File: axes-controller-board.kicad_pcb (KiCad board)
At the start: 4 copper layers, 203.1 x 102.9 mm, 173 parts, among them IC1 TPS5450QDDARQ1, IC2 ACS37800KMACTR-030B3-SPI, IC3 ACS37800KMACTR-030B3-SPI, IC4 ACS37800KMACTR-030B3-SPI, IC5 STM32H723ZGT6, J1 Conn_ST_STDC14, J10 Conn_01x08, J11 Conn_01x04, J12 Conn_01x08, J13 Conn_01x04, J14 Conn_01x08, J15 Conn_01x08, J16 Conn_01x04, J17 Conn_01x08, J18 Conn_01x08, J19 Conn_01x04, J2 Conn_01x03, J20 Conn_01x08, J21 Conn_01x08, J22 Conn_01x04, J23 Conn_01x08, J24 Conn_01x08, J25 Conn_01x04, J26 Conn_01x08, J27 Raspberry_Pi_2_3, J28 DC1, J29 DC2, J3 Conn_01x03, J30 DC3, J31 Conn_01x08, J32 Conn_01x08, J33 DC1, J34 Conn_01x08, J35 Conn_01x08, J36 Conn_01x08, J37 ENDSTOP, J38 ENDSTOP, J39 ENDSTOP, J4 Conn_01x03, J40 Conn_01x03, J41 ENDSTOP, J42 ENDSTOP, J5 DRIVER, J6 NTC, J7 DRIVER, J8 NTC, J9 Conn_01x08, SW1 RESET, U1 LM1117MP-3.3, U3 UA9637A, U5 UA9637A, U7 UA9637A, Y1 16MHz

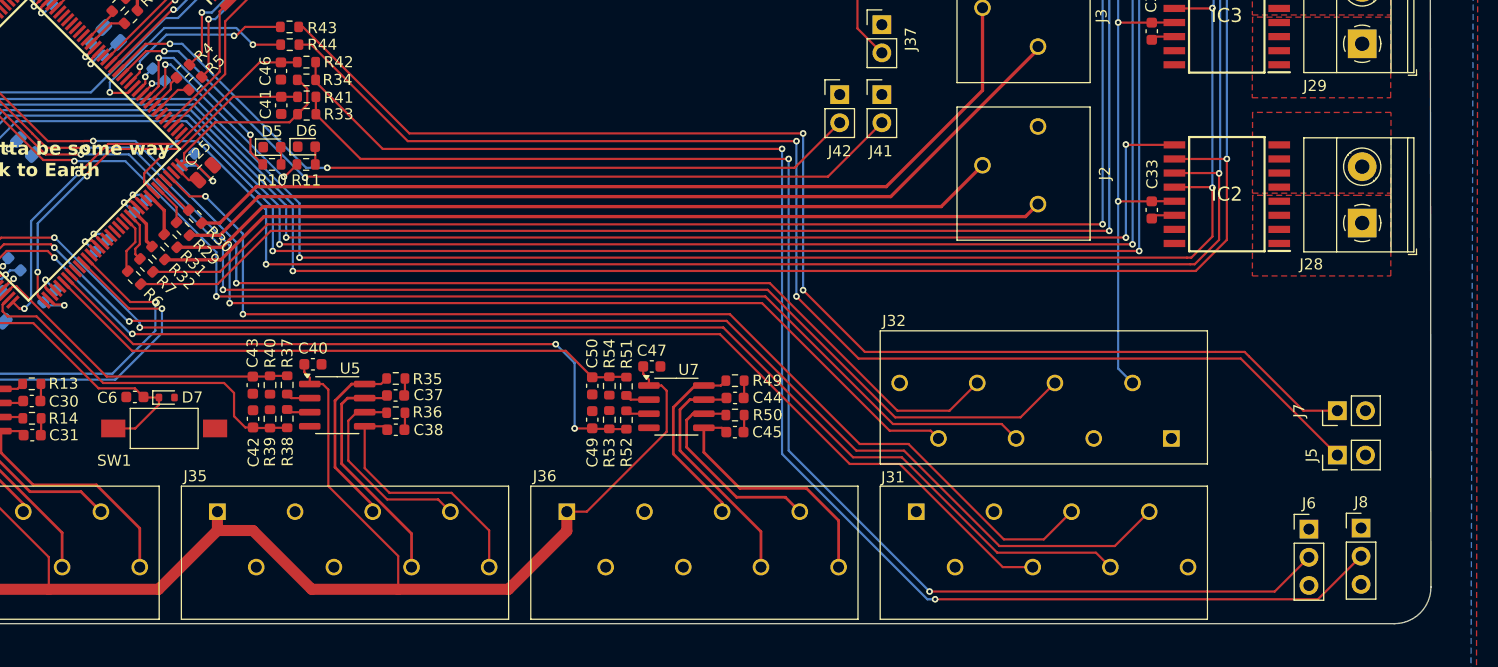
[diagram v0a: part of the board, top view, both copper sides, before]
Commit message: fix: nozzle and hb connector
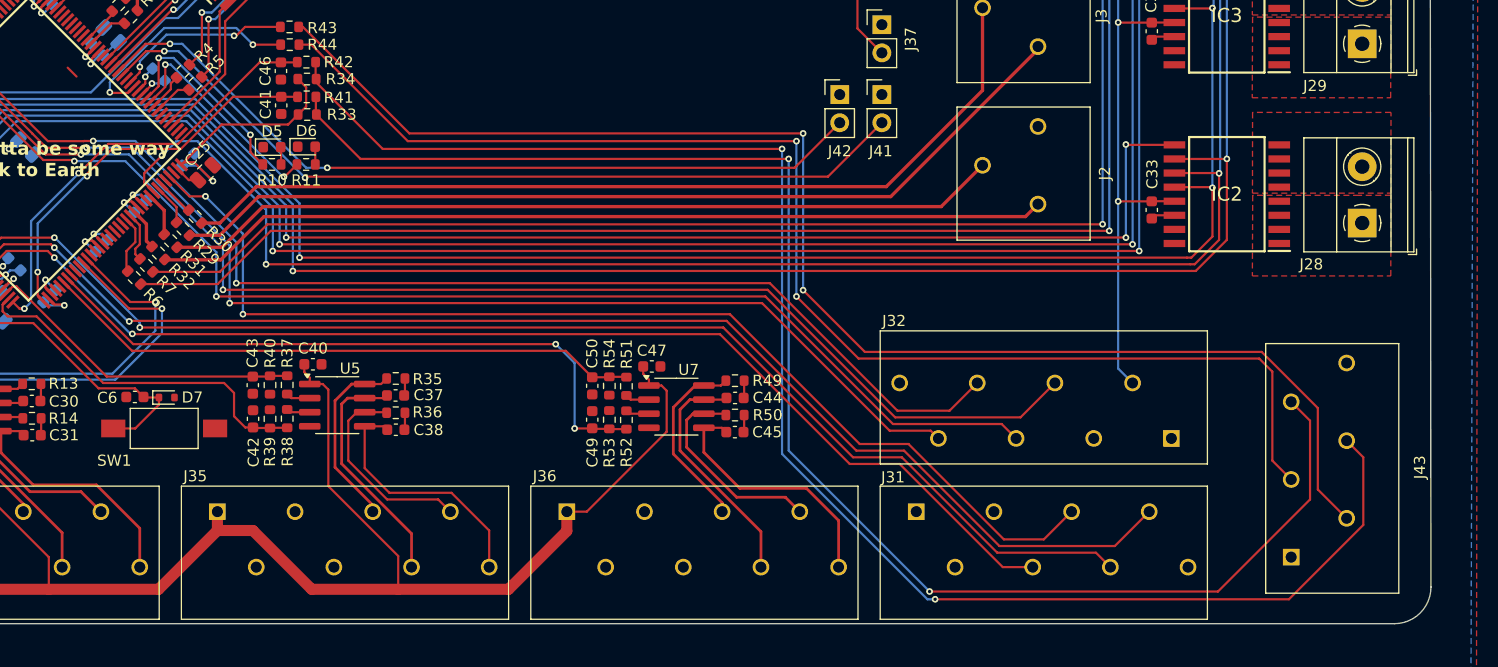
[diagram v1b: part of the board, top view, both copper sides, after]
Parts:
- removed J5, J7: DRIVER, Connector_PinHeader_2.54mm:PinHeader_1x02_P2.54mm_Vertical
- removed J6, J8: NTC, Connector_PinHeader_2.54mm:PinHeader_1x03_P2.54mm_Vertical
- added J43: Conn_01x06, Local:1985234, F.Cu at (250.3, 139.0)
- moved R34 0.09 mm to (161.6, 95.9), turned to 0 degrees
- moved R33 0.06 mm to (161.6, 99.1), turned to 0 degrees
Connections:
- R33 pad 1: Net-(J6-Pin_2) -> +3V3
- R33 pad 2: +3V3 -> Net-(J43-Pin_5)
- R34 pad 1: Net-(J8-Pin_2) -> +3V3
- R34 pad 2: +3V3 -> Net-(J43-Pin_4)
- R41 pad 2: Net-(J6-Pin_2) -> Net-(J43-Pin_5)
- R42 pad 2: Net-(J8-Pin_2) -> Net-(J43-Pin_4)
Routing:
- net Net-(J43-Pin_4): track 0.00 -> 142.7 mm, vias 0 -> 2
- net Net-(J43-Pin_5): track 0.00 -> 137.4 mm, vias 0 -> 2
- net Net-(J8-Pin_2): track 133.1 -> 0.00 mm, vias 2 -> 0
- net Net-(J6-Pin_2): track 125.6 -> 0.00 mm, vias 2 -> 0
- net /N_PWM: track 116.2 -> 125.4 mm
- net /H_PWM: track 117.1 -> 118.6 mm
- net GND: track 51.6 -> 52.7 mm

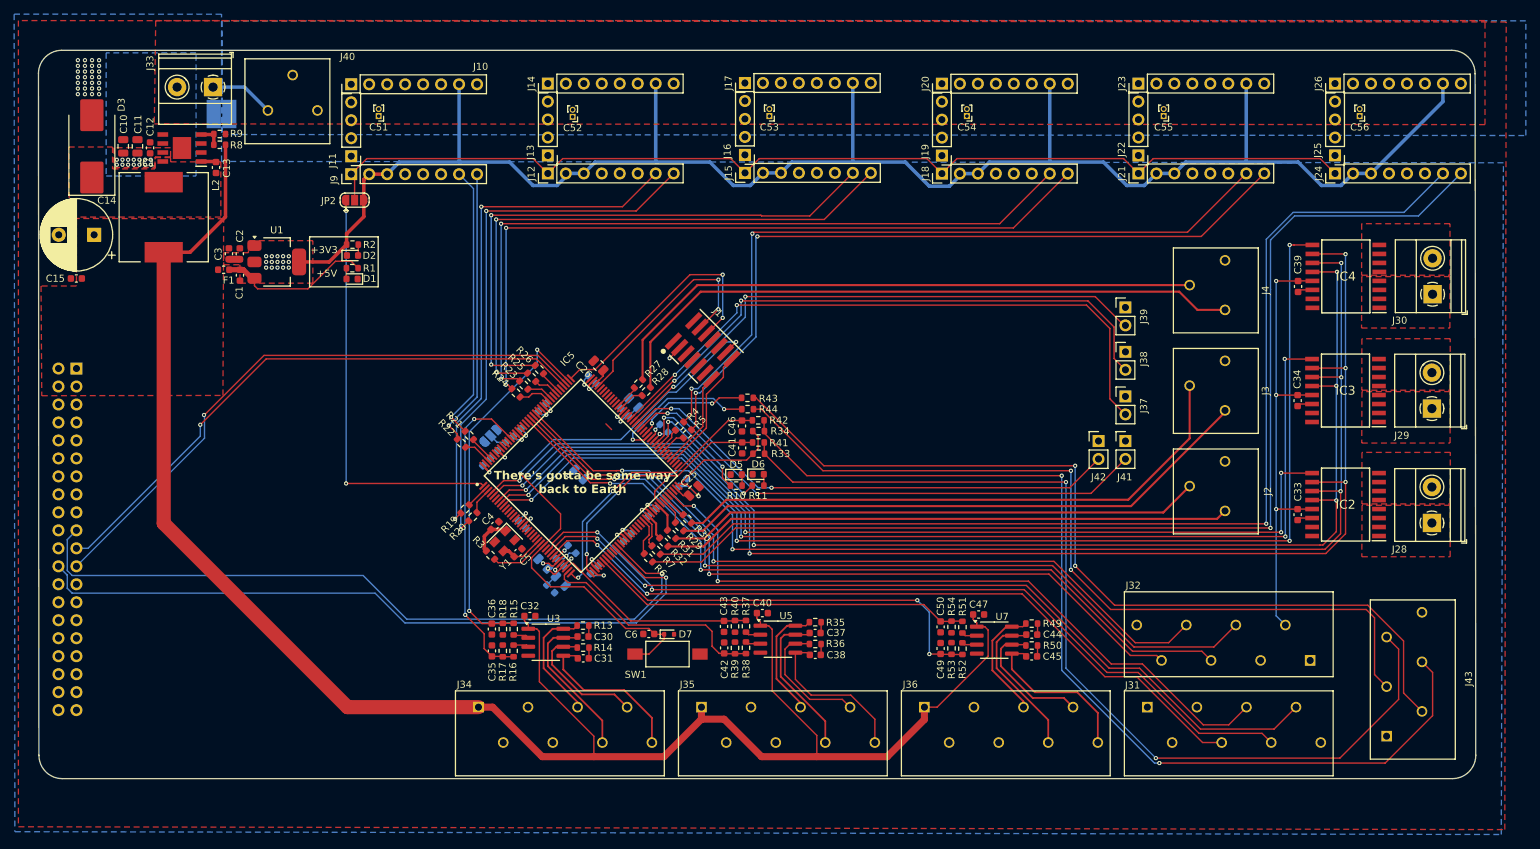
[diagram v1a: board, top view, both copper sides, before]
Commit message: fix: 3d 6 pin connector libs, fix DRC
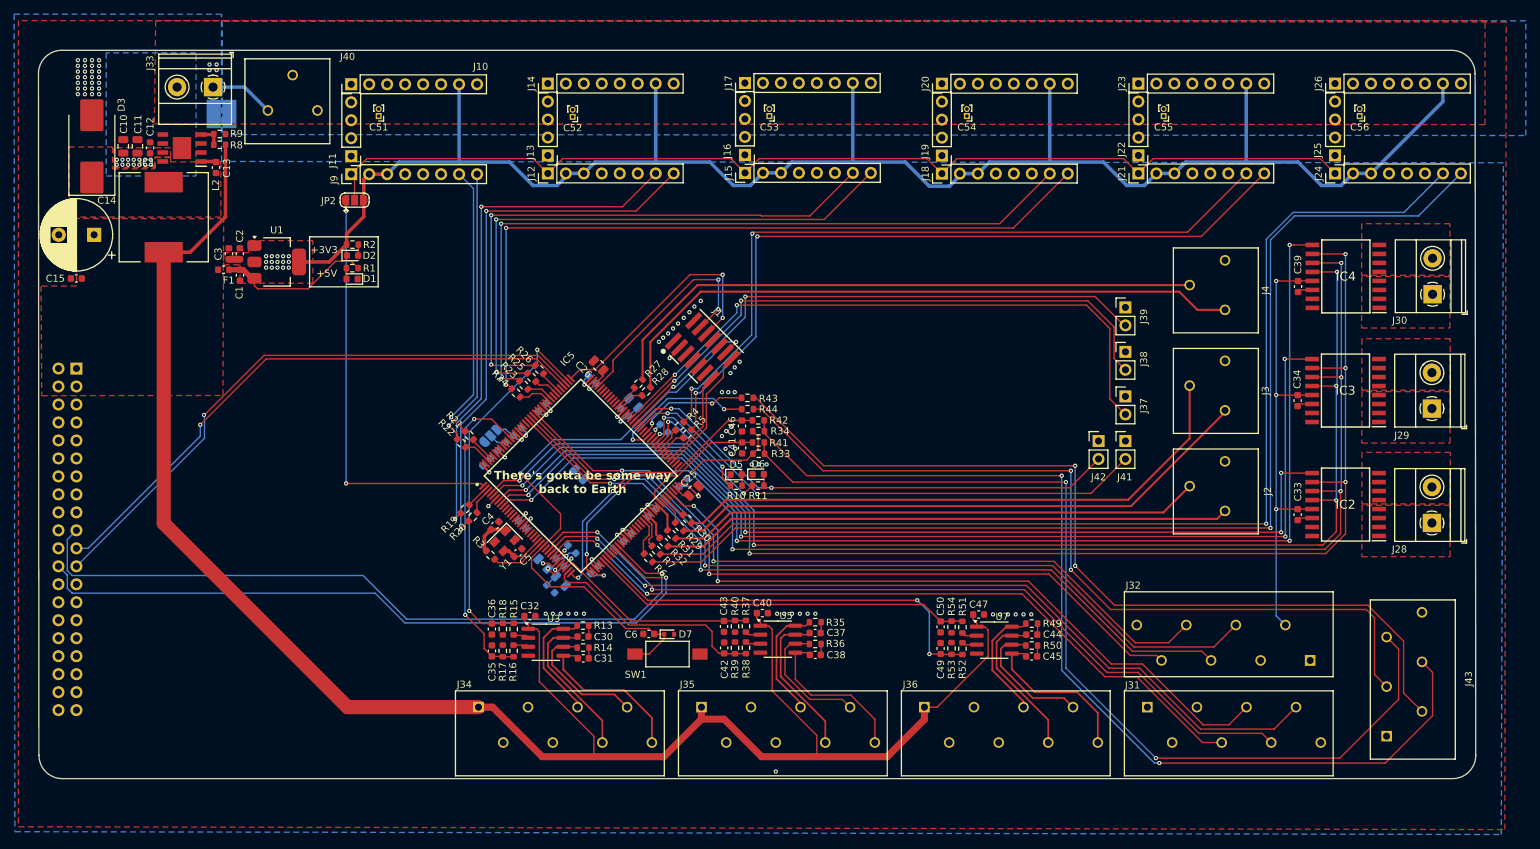
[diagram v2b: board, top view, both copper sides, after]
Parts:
- moved C18 0.16 mm to (127.5, 96.0)
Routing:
- net +3V3: track 381.7 -> 385.9 mm, vias 35 -> 36
- net GND: track 52.7 -> 51.7 mm, vias 39 -> 90

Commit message: feat: mounting holes
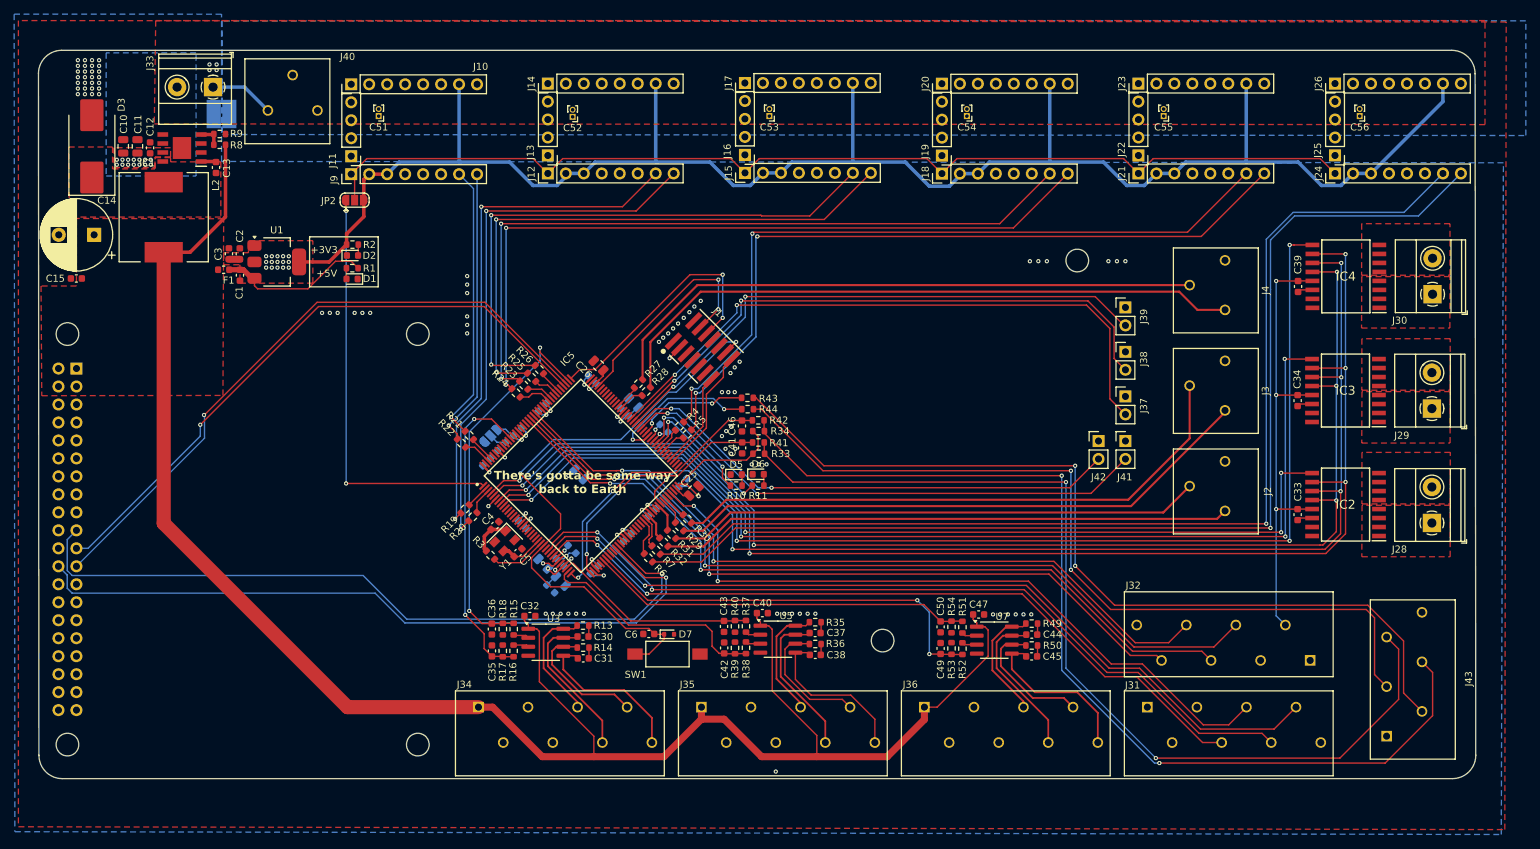
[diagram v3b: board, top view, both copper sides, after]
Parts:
- added H3: MountingHole, Local:MountingHole_3.2mm_M3_ISO14580, F.Cu at (63.9, 140.2)
- added H4: MountingHole, Local:MountingHole_3.2mm_M3_ISO14580, F.Cu at (113.4, 140.2)
- added H5: MountingHole, Local:MountingHole_3.2mm_M3_ISO14580, F.Cu at (113.4, 82.2)
- added H6: MountingHole, Local:MountingHole_3.2mm_M3_ISO14580, F.Cu at (63.9, 82.2)
- added H7: MountingHole, Local:MountingHole_3.2mm_M3_ISO14580, F.Cu at (206.6, 71.8)
- added H8: MountingHole, Local:MountingHole_3.2mm_M3_ISO14580, F.Cu at (179.1, 125.5)
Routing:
- net /MCU/SPI3_SCK: track 85.2 -> 91.4 mm
- net /MCU/SPI3_MISO: track 82.4 -> 88.5 mm
- net /MCU/MX_A: track 54.1 -> 54.7 mm
- net GND: vias 90 -> 108

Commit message: feat: matrix cit
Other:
- board text added: "The spice must flow"
- board text added: "{dblquote}Because you didn't come here to make the choiche, you've already made it. You're here to try to understand why you made it{dblquote}"
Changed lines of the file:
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@@
 		(layer "Edge.Cuts")
+	)
+	(gr_text "The spice must flow"
+		(at 122.8 63.8 0)
+		(layer "F.SilkS")
+		(effects
+			(font
+				(size 1 1)
+				(thickness 0.15)
+			)
+			(justify left bottom)
+		)
 	)
 	(gr_text "+5V"
@@
 		)
 	)
+	(gr_text "{dblquote}Because you didn't come here to make the choiche,\nyou've already made it.\nYou're here to try to understand why you made it{dblquote}"
+		(at 163.2 88.3 0)
+		(layer "F.SilkS")
+		(effects
+			(font
+				(size 1.1 1.1)
+				(thickness 0.2)
+				(bold yes)
+			)
+			(justify left bottom)
+		)
+	)
